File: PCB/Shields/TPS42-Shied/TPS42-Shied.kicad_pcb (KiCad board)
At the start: 2 copper layers, 32.1 x 17 mm, 9 parts, among them J1 PJ-320A, J2 Conn_01x06, J3 OLED, J4 PJ-320A, J5 Conn_01x06, J6 OLED

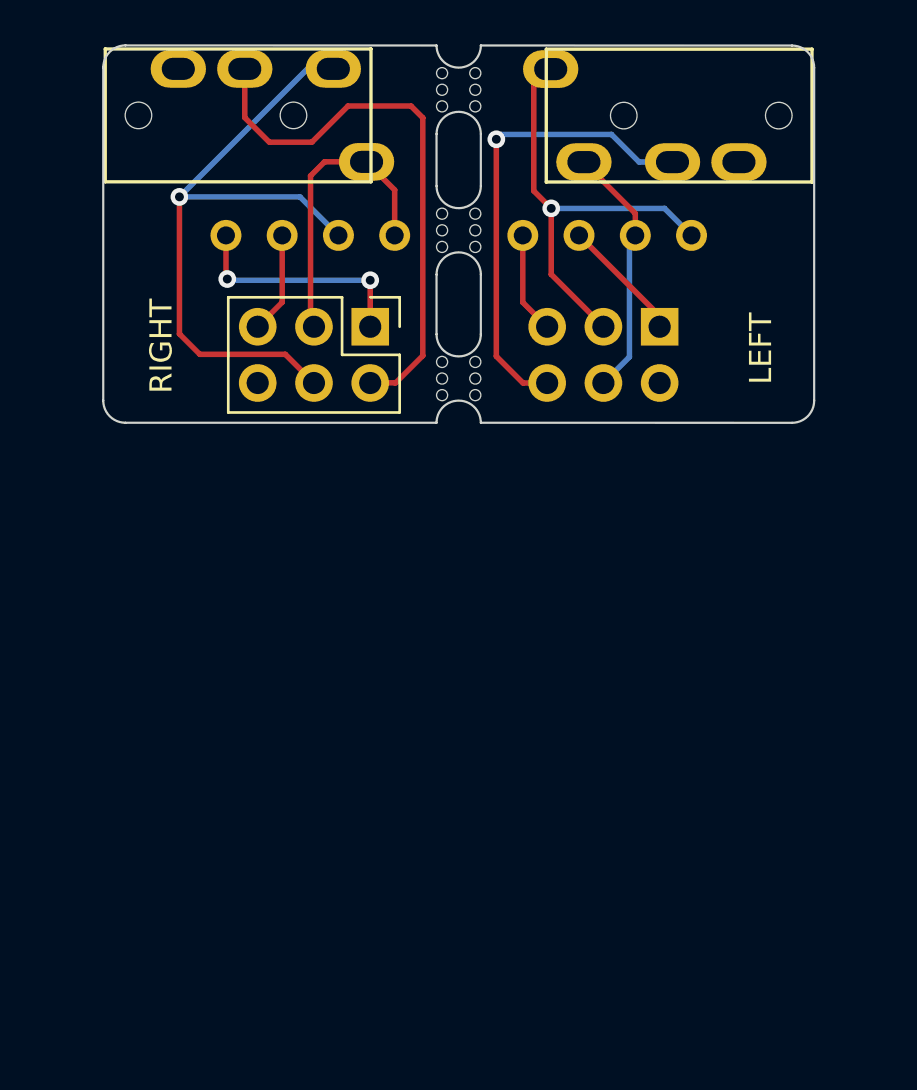
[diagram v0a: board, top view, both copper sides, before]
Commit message: add left lcd shield
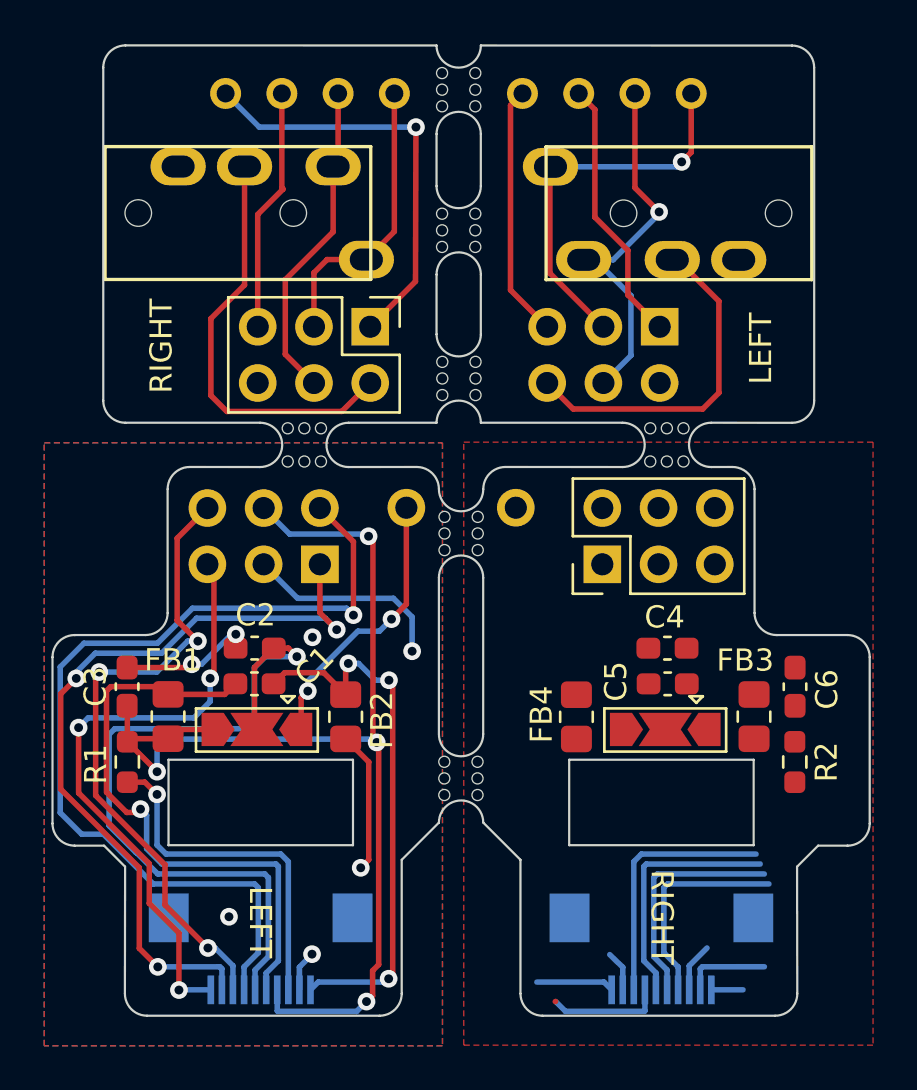
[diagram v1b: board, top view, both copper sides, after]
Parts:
- removed the mouse-bite-2mm-slot at (45.6, 67.9)
- removed the mouse-bite-2mm-slot at (45.6, 54.8)
- added C1: 560pF/680pF, Capacitor_SMD:C_0603_1608Metric_Pad1.08x0.95mm_HandSolder, F.Cu at (36.3, 80.1)
- added C2: 1uF, Capacitor_SMD:C_0603_1608Metric_Pad1.08x0.95mm_HandSolder, F.Cu at (36.3, 81.7)
- added C3: 1uF, Capacitor_SMD:C_0603_1608Metric_Pad1.08x0.95mm_HandSolder, F.Cu at (30.6, 81.8)
- added C4: 560pF/680pF, Capacitor_SMD:C_0603_1608Metric_Pad1.08x0.95mm_HandSolder, F.Cu at (55.0, 80.1)
- added C5: 1uF, Capacitor_SMD:C_0603_1608Metric_Pad1.08x0.95mm_HandSolder, F.Cu at (55.0, 81.7)
- added C6: 1uF, Capacitor_SMD:C_0603_1608Metric_Pad1.08x0.95mm_HandSolder, F.Cu at (60.7, 81.8)
- added FB1: Ferrite_Bead, Resistor_SMD:R_0805_2012Metric_Pad1.20x1.40mm_HandSolder, F.Cu at (32.4, 83.1)
- added FB2: Ferrite_Bead, Resistor_SMD:R_0805_2012Metric_Pad1.20x1.40mm_HandSolder, F.Cu at (40.5, 83.2)
- added FB3: Ferrite_Bead, Resistor_SMD:R_0805_2012Metric_Pad1.20x1.40mm_HandSolder, F.Cu at (58.9, 83.2)
- added FB4: Ferrite_Bead, Resistor_SMD:R_0805_2012Metric_Pad1.20x1.40mm_HandSolder, F.Cu at (50.9, 83.2)
- added J10: FH12-10S-0.5SH, Connector_FFC-FPC:Hirose_FH12-10S-0.5SH_1x10-1MP_P0.50mm_Horizontal, B.Cu at (54.7, 93.6)
- added J11: Conn_01x06, Connector_PinHeader_2.54mm:PinHeader_2x03_P2.54mm_Vertical, F.Cu at (52.0, 76.3)
- added J12: Conn_01x01, Connector_PinHeader_2.54mm:PinHeader_1x01_P2.54mm_Vertical, F.Cu at (48.1, 73.7)
- added J7: FH12-10S-0.5SH, Connector_FFC-FPC:Hirose_FH12-10S-0.5SH_1x10-1MP_P0.50mm_Horizontal, B.Cu at (36.6, 93.6)
- added J8: Conn_01x06, Connector_PinHeader_2.54mm:PinHeader_2x03_P2.54mm_Vertical, B.Cu at (39.3, 76.3)
- added J9: Conn_01x01, Connector_PinHeader_2.54mm:PinHeader_1x01_P2.54mm_Vertical, F.Cu at (43.2, 73.7)
- added JP1: Jumper_3_Open, Jumper:SolderJumper-3_P2.0mm_Open_TrianglePad1.0x1.5mm, F.Cu at (36.4, 83.7)
- added JP2: Jumper_3_Open, Jumper:SolderJumper-3_P2.0mm_Open_TrianglePad1.0x1.5mm, F.Cu at (54.9, 83.7)
- added R1: 10kΩ, Resistor_SMD:R_0603_1608Metric_Pad0.98x0.95mm_HandSolder, F.Cu at (30.6, 85.2)
- added R2: 10kΩ, Resistor_SMD:R_0603_1608Metric_Pad0.98x0.95mm_HandSolder, F.Cu at (60.7, 85.2)
- added mouse-bite-2mm-slot: VAL**, TPS42-Shield:mouse-bite-2mm-slot, F.Cu at (45.7, 85.9)
- added mouse-bite-2mm-slot: VAL**, TPS42-Shield:mouse-bite-2mm-slot, F.Cu at (45.6, 67.9)
- added mouse-bite-2mm-slot: VAL**, TPS42-Shield:mouse-bite-2mm-slot, F.Cu at (45.6, 54.8)
- added mouse-bite-2mm-slot: VAL**, TPS42-Shield:mouse-bite-2mm-slot, F.Cu at (45.7, 74.9)
- added mouse-bite-2mm-slot: VAL**, TPS42-Shield:mouse-bite-2mm-slot, F.Cu at (55.0, 70.9)
- added mouse-bite-2mm-slot: VAL**, TPS42-Shield:mouse-bite-2mm-slot, F.Cu at (38.6, 70.9)
- moved J3 6.41 mm to (38.8, 55.0)
- moved J6 6.41 mm to (52.2, 55.0)
- moved J4 4.41 mm to (61.5, 58.7)
- moved J1 4.41 mm to (29.6, 62.2)
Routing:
- net +3V3: track 0.00 -> 60.8 mm, vias 0 -> 4
- net /L_EIN: track 0.00 -> 41.7 mm, vias 0 -> 1
- net VDDA: track 0.00 -> 37.2 mm, vias 0 -> 1
- net /L_DAT: track 0.00 -> 35.5 mm, vias 0 -> 3
- net /L_DISP: track 0.00 -> 34.2 mm, vias 0 -> 1
- net /L_CS: track 0.00 -> 29.2 mm, vias 0 -> 3
- net /L_CLK: track 0.00 -> 28.0 mm, vias 0 -> 3
- net GND: track 0.00 -> 26.9 mm, vias 0 -> 7
- net GNDA: track 0.00 -> 26.3 mm, vias 0 -> 3
- net /L_EXTMODE: track 0.00 -> 15.9 mm, vias 0 -> 1
- net Net-(J1-Pad1): track 30.4 -> 14.6 mm, vias 1 -> 0
- net Net-(J9-Pad1): track 0.00 -> 12.6 mm, vias 0 -> 2
- net /R_DISP: track 0.00 -> 11.7 mm
- net /R_CS: track 0.00 -> 11.5 mm
- net Net-(J2-Pad1): track 10.6 -> 19.1 mm, vias 2 -> 1
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- added copper zone on B.Cu, net GND
- added copper zone on F.Cu, net GND
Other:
- board size 32.1 x 17 mm -> 36.9 x 43.8 mm
